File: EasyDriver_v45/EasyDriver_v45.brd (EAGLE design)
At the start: 48.3 x 20.3 mm, 44 parts, among them IC1 A3967SLB, IC2 V_REG_317SMD

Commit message: Version 4.5 updates -
* All Rs and Cs are now normal 0603 SparkFun footprints
* Added series Rs and pull downs for STEP and DIR inputs
* Updated pot footprint to TRIMPOT-3MM-2 for better soldering
* Switched license from CC BY 3.0 to CC BY-SA 3.0
* Fixed pot direction silk screen
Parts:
- R16: value TRIMPOT-2 -> 10K; device SparkFun-Electromechanical:TRIMPOT_TC33 -> SparkFun-Electromechanical:TRIMPOT-3MM-2
- R20, R21: device SparkFun03_30_09:C0402 -> SparkFun-Resistors:0603-RES
- moved R20 0.36 mm to (39.4, 6.48)
- moved R21 0.13 mm to (38.1, 1.78)
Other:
- board text added: "+"
- board text removed: "MAX"
- board text removed: "MIN"

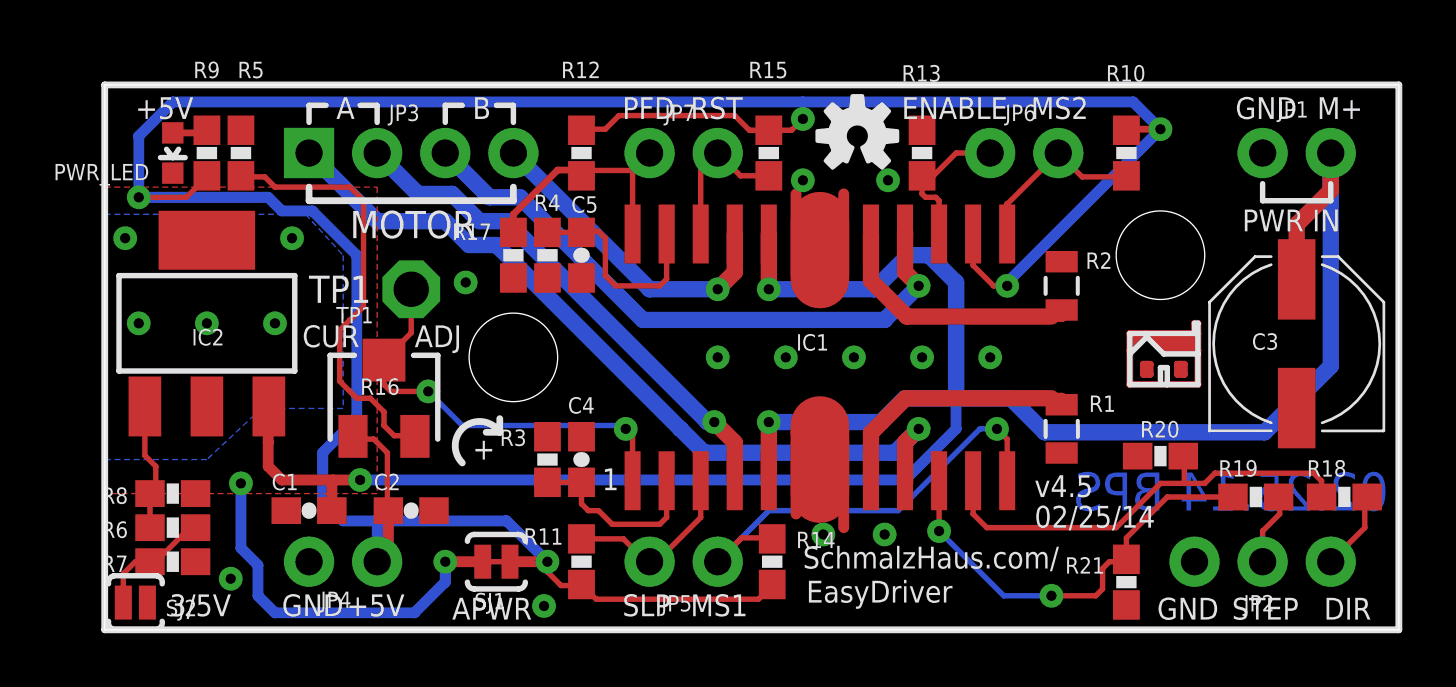
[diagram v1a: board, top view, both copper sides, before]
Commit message: Small updates to schematic and board
* Rotated ground symbol on schematic so it matched other ground symbols
* Changed TP1 to standard SparkFun test point footprint
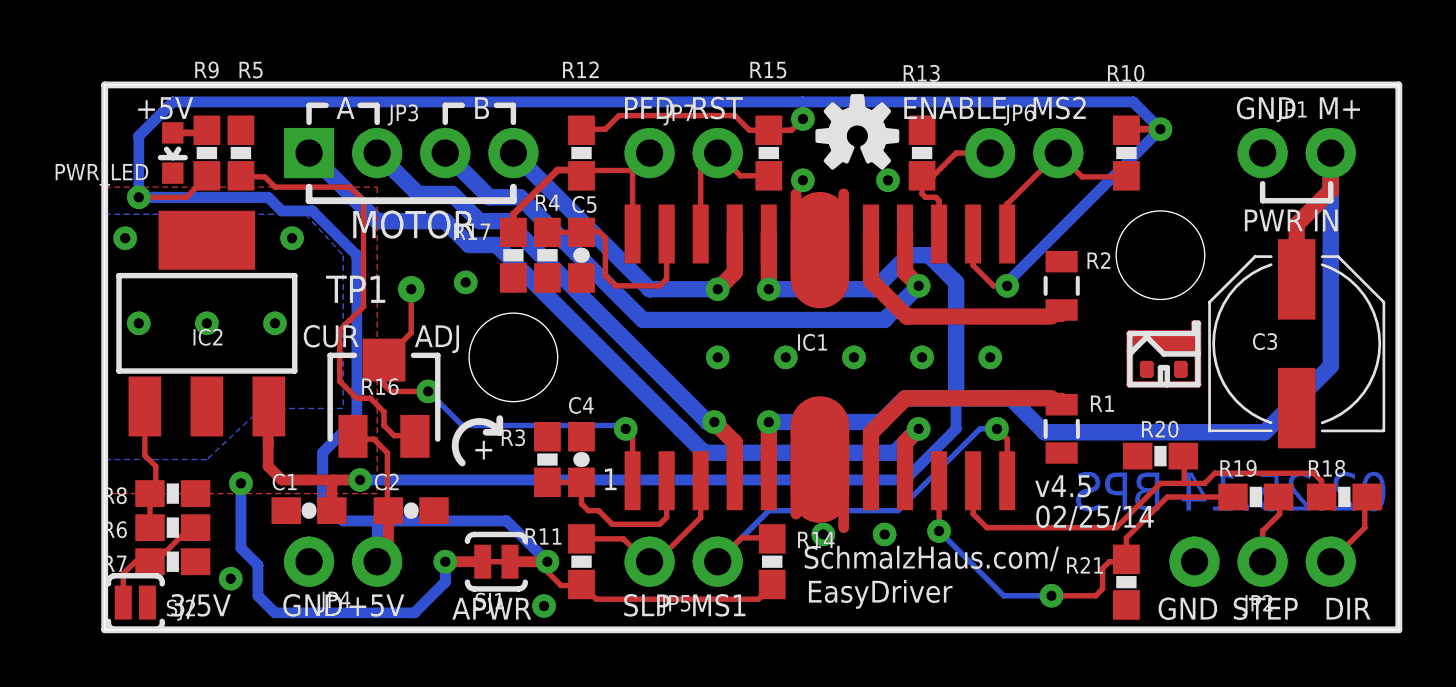
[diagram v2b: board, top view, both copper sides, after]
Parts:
- TP1: value TPPAD1-13 -> TEST-POINTTP_15TH_THRU; device testpad:P1-13 -> SparkFun-Passives:TP_15TH
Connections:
- net N$12: now also TP1.P$1; no longer TP1.1
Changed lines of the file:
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@@
 <text x="18.542" y="5.207" size="0.8128" layer="21" font="vector" ratio="18">1</text>
 <text x="13.716" y="6.35" size="0.8128" layer="21" font="vector" ratio="18">+</text>
-<text x="7.62" y="12.192" size="1.016" layer="21" font="vector" ratio="18">TP1</text>
+<text x="8.255" y="12.192" size="1.016" layer="21" font="vector" ratio="18">TP1</text>
 <text x="11.557" y="10.541" size="0.8128" layer="21" font="vector" ratio="18">ADJ</text>
 <polygon width="0.254" layer="42">
@@
 <attribute name="VALUE" x="12.8905" y="12.827" size="0.6096" layer="27"/>
 </element>
-<element name="TP1" library="testpad" package="P1-13" value="TPPAD1-13" x="11.43" y="12.7" smashed="yes">
-<attribute name="NAME" x="8.636" y="11.43" size="0.6096" layer="25" ratio="10"/>
-<attribute name="VALUE" x="8.636" y="10.668" size="0.6096" layer="27"/>
-</element>
 <element name="JP8" library="SparkFun-7-28-09" package="STAND-OFF" value="STAND-OFF" x="39.37" y="13.97" smashed="yes"/>
 <element name="JP9" library="SparkFun-7-28-09" package="STAND-OFF" value="STAND-OFF" x="15.24" y="10.16" smashed="yes"/>
@@
 <attribute name="VALUE" x="35.8775" y="0.889" size="0.6096" layer="27"/>
 </element>
+<element name="TP1" library="SparkFun-Passives" package="TP_15TH" value="TEST-POINTTP_15TH_THRU" x="11.43" y="12.7"/>
 </elements>
 <signals>
@@
 <contactref element="IC1" pad="1"/>
 <contactref element="R16" pad="2"/>
-<contactref element="TP1" pad="1"/>
 <wire x1="19.685" y1="7.239" x2="19.685" y2="5.56" width="0.2032" layer="1"/>
 <wire x1="19.431" y1="7.493" x2="19.685" y2="7.239" width="0.2032" layer="1"/>
@@
 <wire x1="11.43" y1="12.7" x2="11.43" y2="11.0734" width="0.2032" layer="1"/>
 <wire x1="11.43" y1="11.0734" x2="10.414" y2="10.0574" width="0.2032" layer="1"/>
+<contactref element="TP1" pad="P$1"/>
 </signal>
 <signal name="N$6">
@@
 <wire x1="37.211" y1="2.286" x2="37.465" y2="2.54" width="0.2032" layer="1"/>
 <wire x1="37.465" y1="2.54" x2="38.061" y2="2.54" width="0.2032" layer="1"/>
-<wire x1="38.061" y1="2.54" x2="38.1" y2="2.628" width="0.2032" layer="1"/>
+<wire x1="38.1" y1="2.628" x2="38.061" y2="2.628" width="0.4064" layer="1"/>
+<wire x1="38.061" y1="2.628" x2="38.061" y2="2.54" width="0.4064" layer="1"/>
 </signal>
 <signal name="SLEEP">

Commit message: * Made TP1 bigger, and no longer covered with solder mask * Switched R5 to 2.4K Ohms to allow Vref down to 1V into driver * Set R17 to 6.8K to allow PFD input to select 'mixed-decay' mode * Swapped location of STEP and DIR series resistors so that pull downs now happen before series Rs. * Suggest SparkFun adjust current limit pot to 2V (measured by TP1) at final test.
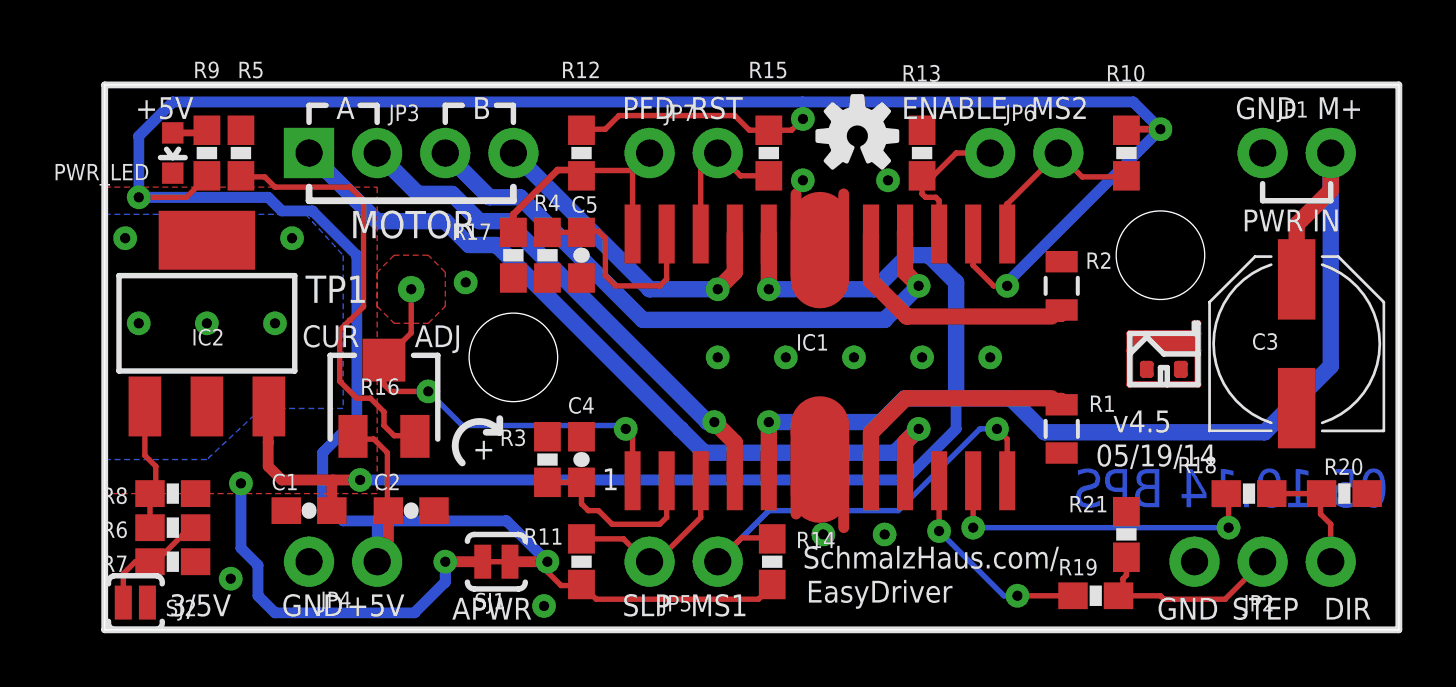
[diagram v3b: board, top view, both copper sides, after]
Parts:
- R17: value ??? -> 6.8K
- R5: value 5.1K -> 2.4K
- moved R19 7.01 mm to (37.0, 1.27)
- moved R20 7.00 mm to (46.2, 5.08), turned to 180 degrees
- moved R18 3.56 mm to (42.7, 5.08)
- moved R21 1.78 mm to (38.1, 3.56), turned to 270 degrees
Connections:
- net N$12 renamed VREF
- net DIR: no longer R20.2
- net DIR_IN: now also R20.2
- net STEP: no longer R21.2
- net STEP_IN: now also R21.2
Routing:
- net STEP: track 16.3 -> 7.87 mm
- net STEP_IN: track 2.69 -> 7.56 mm
- net DIR: track 17.1 -> 12.6 mm, vias 0 -> 2
- net DIR_IN: track 2.98 -> 4.57 mm
- added copper zone on layer 1, net VREF
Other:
- board text added: "05.19.14 BPS"
- board text added: "05/19/14"
- board text removed: "02.25.14 BPS"
- board text removed: "02/25/14"

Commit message: Based on SparkFun feedback * Replaced frame with newest version from SparkFun library * Replaced VCC symbol with newest version from SparkFun library * Move components so that keepout area around mounding holes is honored.
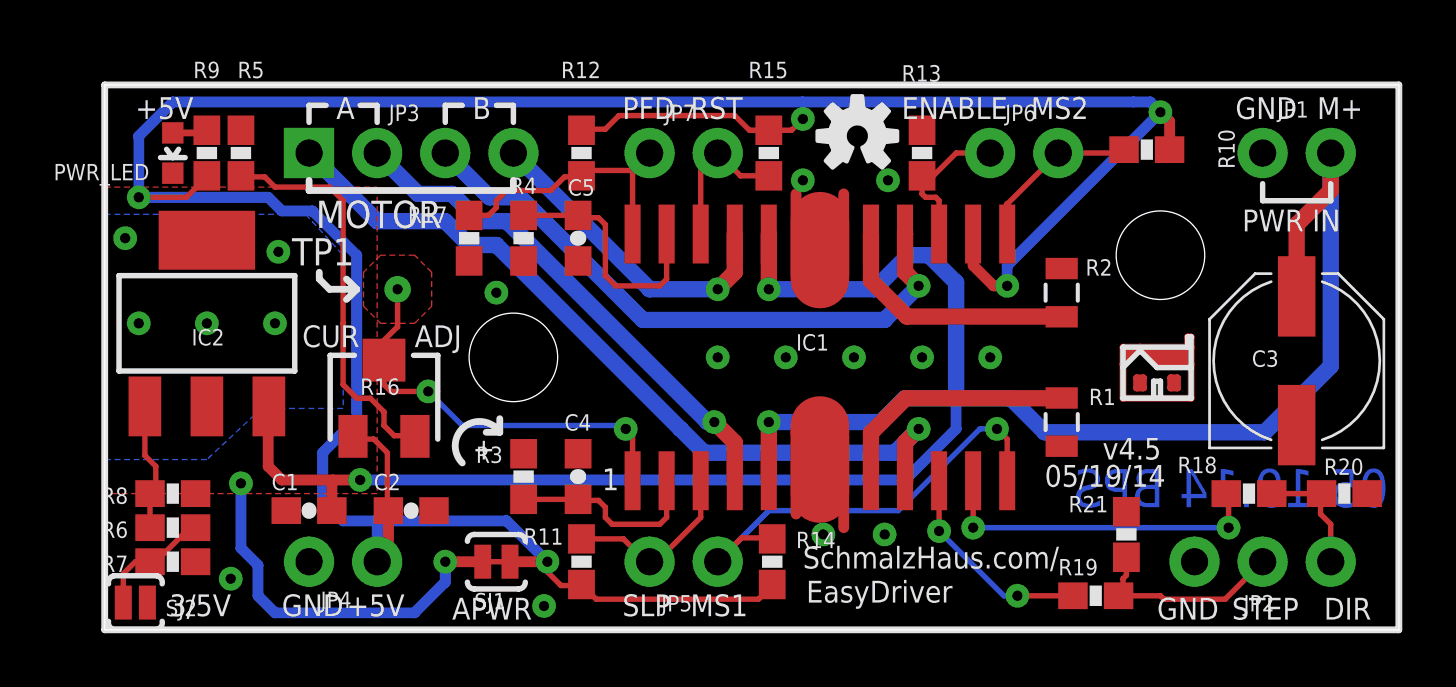
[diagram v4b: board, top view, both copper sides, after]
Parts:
- added FRAME2: FRAME-LETTER, SparkFun-Aesthetics:CREATIVE_COMMONS
- moved R17 1.77 mm to (13.6, 14.6)
- moved R3 1.09 mm to (15.6, 5.71)
- moved R4 1.09 mm to (15.6, 14.6)
- moved R10 0.77 mm to (38.9, 17.9), turned to 0 degrees
- moved C4 0.65 mm to (17.7, 5.71)
- moved C5 0.65 mm to (17.7, 14.6)
- moved C3 0.63 mm to (44.5, 10.0)
- moved U$1 0.57 mm to (39.2, 8.64)
- moved TP1 0.51 mm to (10.9, 12.7)
- moved R1 0.25 mm to (35.7, 7.75)
- moved R2 0.25 mm to (35.7, 12.6)
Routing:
- net N$7: track 7.91 -> 9.32 mm
- net N$11: track 16.0 -> 14.8 mm
- net PFD: track 9.35 -> 10.4 mm
- net V+: track 83.8 -> 84.4 mm
- net VCC: track 112.3 -> 112.9 mm
